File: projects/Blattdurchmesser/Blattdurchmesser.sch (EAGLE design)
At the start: 14 parts, among them K1 TX2_RELAY", U1 ARDUINOR3-DIMENSION

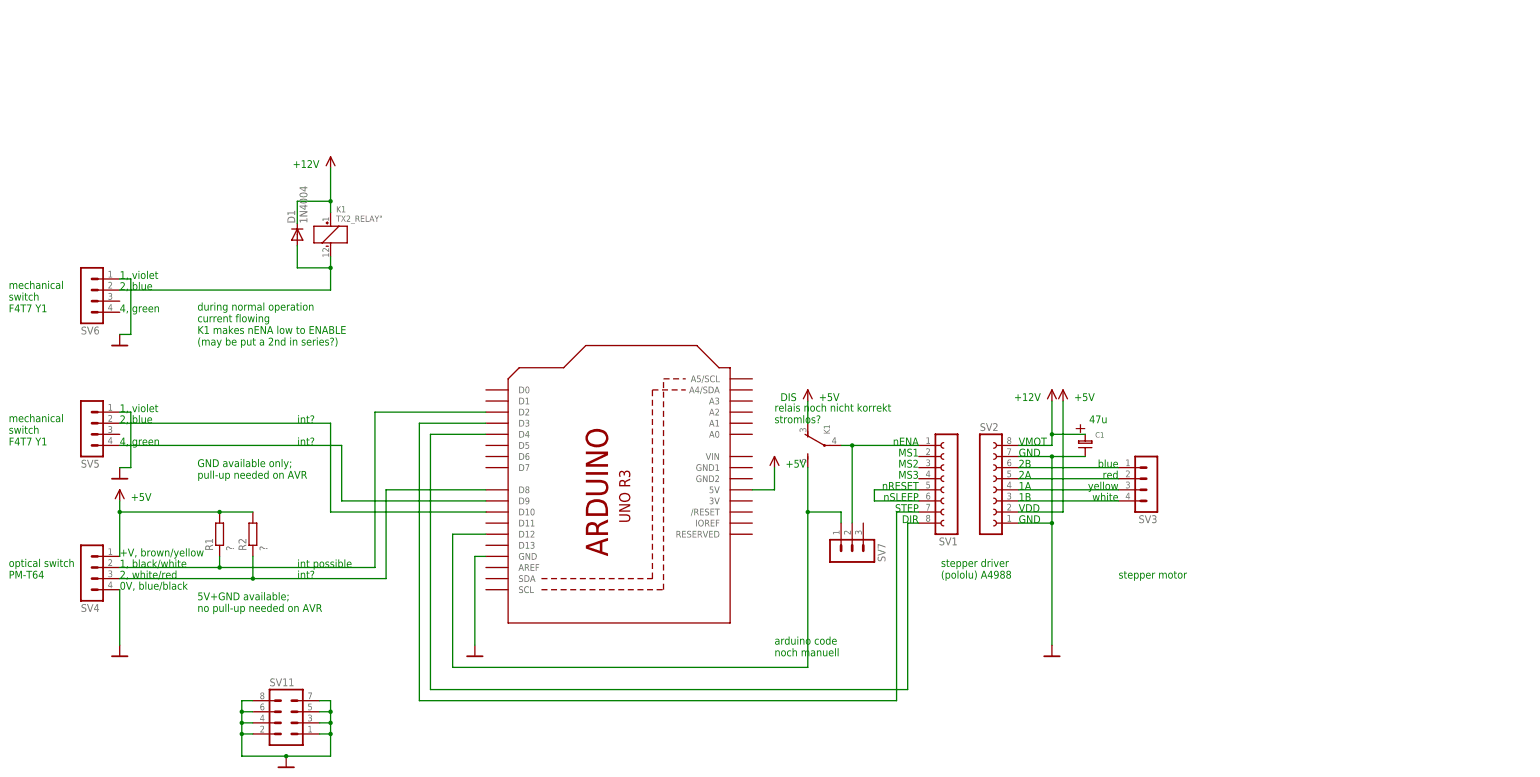
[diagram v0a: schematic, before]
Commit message: improvement; * replace arduino part/footprint by one that does                not have milling slots              * avoid using a relais as it has disadvantages
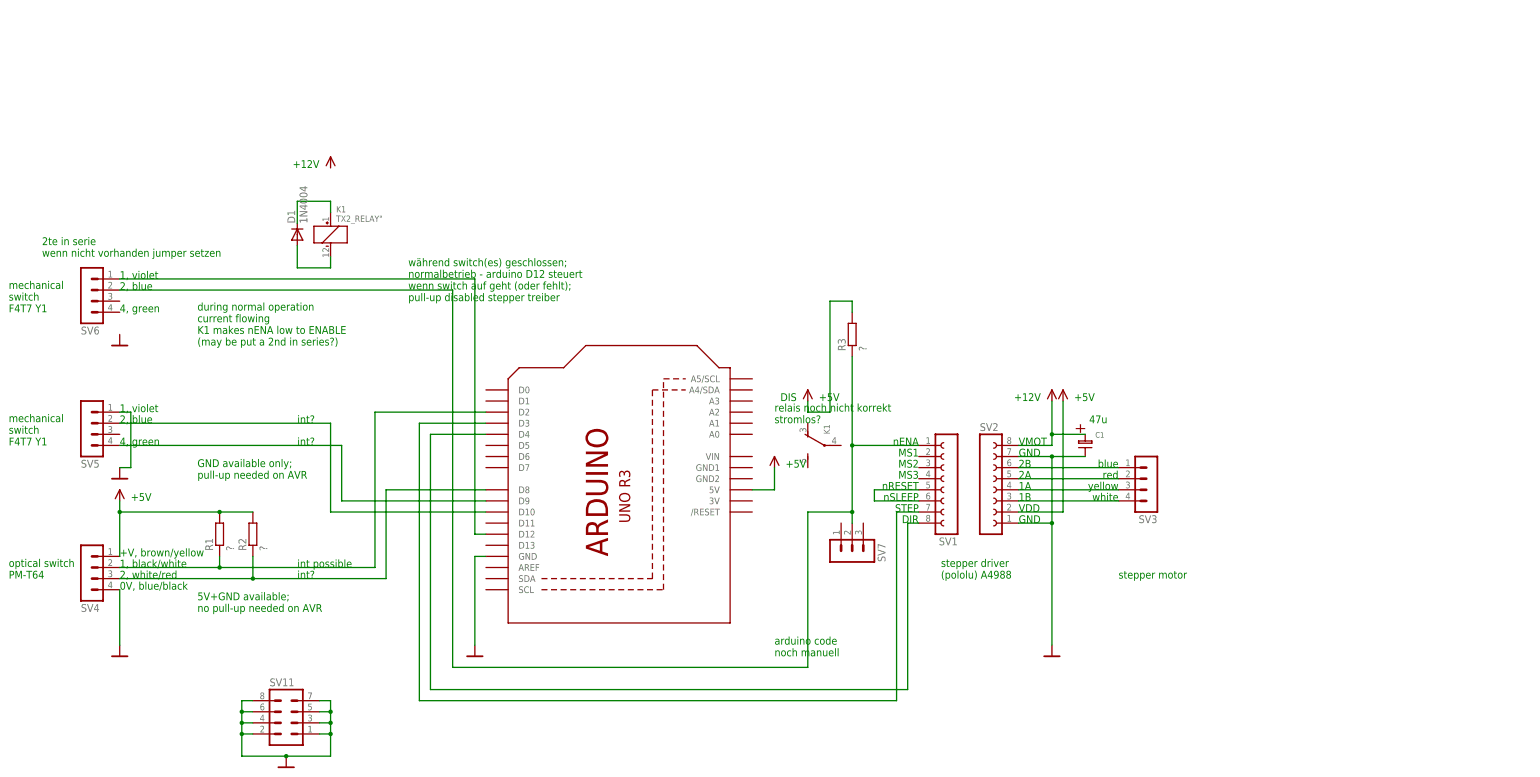
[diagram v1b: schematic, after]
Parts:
- removed U1: ARDUINOR3-DIMENSION, adafruit:ARDUINOR3-DIMENSION
- added Q1: ARDUINOR3-NOIOREF-NOTEXT, adafruit:ARDUINOR3-NOIOREF-NOTEXT
- added R3: ?, rcl:R-EU_0207/10
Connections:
- removed net N$10: K1TX2_SWITCH.P, SV1.1, SV7.2
- new net N$16: D1.C, K1TX2_COIL.+
- new net N$8: D1.A, K1TX2_COIL.-
- net +12V: no longer D1.C, K1TX2_COIL.+
- net +5V: now also Q1.5V, R3.2; no longer K1TX2_SWITCH.O, U1.5V
- net GND: now also Q1.GND; no longer SV6.1, U1.GND
- net N$1: now also Q1.D4; no longer U1.D4
- net N$11: now also Q1.D12, SV6.1; no longer D1.A, K1TX2_COIL.-, SV6.2
- net N$12: now also Q1.D10; no longer U1.D10
- net N$13: now also Q1.D9; no longer U1.D9
- net N$14: now also R3.1, SV1.1, SV6.2, SV7.2; no longer K1TX2_SWITCH.S, SV7.1, U1.D12
- net N$15: now also Q1.D2; no longer U1.D2
- net N$2: now also Q1.D3; no longer U1.D3
- net N$9: now also Q1.D8; no longer U1.D8
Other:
- note added: "2te in serie wenn nicht vorhanden jumper setzen"
- note added: "während switch(es) geschlossen; normalbetrieb - arduino D12 steuert wenn switch auf geht (oder fehlt); pull-up disabled stepper treiber"
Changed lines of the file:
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@@
 </classes>
 <parts>
-<part name="U1" library="adafruit" deviceset="ARDUINOR3" device="-DIMENSION"/>
 <part name="K1" library="relay" deviceset="TX2_RELAY" device="&quot;"/>
 <part name="SV1" library="con-lsta" deviceset="FE08-1" device=""/>
@@
 <part name="D1" library="diode" deviceset="1N4004" device=""/>
 <part name="SV7" library="con-lstb" deviceset="MA03-1" device=""/>
+<part name="R3" library="rcl" deviceset="R-EU_" device="0207/10" value="?"/>
+<part name="Q1" library="adafruit" deviceset="ARDUINOR3-NOIOREF" device="-NOTEXT"/>
 </parts>
 <sheets>
@@
 <text x="119.38" y="50.8" size="1.778" layer="91">relais noch nicht korrekt
 stromlos?</text>
+<text x="35.56" y="78.74" size="1.778" layer="91">während switch(es) geschlossen;
+normalbetrieb - arduino D12 steuert
+wenn switch auf geht (oder fehlt);
+pull-up disabled stepper treiber</text>
+<text x="-48.26" y="88.9" size="1.778" layer="91">2te in serie
+wenn nicht vorhanden jumper setzen</text>
 </plain>
 <instances>
-<instance part="U1" gate="G$1" x="83.82" y="38.1" rot="R90"/>
 <instance part="K1" gate="TX2_COIL" x="17.78" y="93.98"/>
 <instance part="K1" gate="TX2_SWITCH" x="132.08" y="45.72" rot="R90"/>
@@
 <instance part="D1" gate="1" x="10.16" y="93.98" rot="R90"/>
 <instance part="SV7" gate="G$1" x="137.16" y="20.32" rot="MR90"/>
+<instance part="R3" gate="G$1" x="137.16" y="71.12" rot="R90"/>
+<instance part="Q1" gate="G$1" x="83.82" y="38.1" rot="R90"/>
 </instances>
 <busses>
@@
 <pinref part="U$3" gate="1" pin="GND"/>
 <wire x1="50.8" y1="0" x2="50.8" y2="20.32" width="0.1524" layer="91"/>
-<pinref part="U1" gate="G$1" pin="GND"/>
 <wire x1="50.8" y1="20.32" x2="53.34" y2="20.32" width="0.1524" layer="91"/>
+<pinref part="Q1" gate="G$1" pin="GND"/>
 </segment>
 <segment>
@@
 <junction x="7.62" y="-25.4"/>
 </segment>
-<segment>
-<pinref part="SV6" gate="1" pin="1"/>
-<wire x1="-30.48" y1="83.82" x2="-27.94" y2="83.82" width="0.1524" layer="91"/>
-<wire x1="-27.94" y1="83.82" x2="-27.94" y2="71.12" width="0.1524" layer="91"/>
-<pinref part="U$12" gate="1" pin="GND"/>
-<wire x1="-27.94" y1="71.12" x2="-30.48" y2="71.12" width="0.1524" layer="91"/>
-</segment>
 </net>
 <net name="+5V" class="0">
@@
 </segment>
 <segment>
-<pinref part="U1" gate="G$1" pin="5V"/>
 <pinref part="U$7" gate="1" pin="+5V"/>
-<wire x1="114.3" y1="35.56" x2="119.38" y2="35.56" width="0.1524" layer="91"/>
 <wire x1="119.38" y1="35.56" x2="119.38" y2="40.64" width="0.1524" layer="91"/>
+<pinref part="Q1" gate="G$1" pin="5V"/>
+<wire x1="119.38" y1="35.56" x2="114.3" y2="35.56" width="0.1524" layer="91"/>
 </segment>
 <segment>
@@
 <segment>
 <pinref part="U$8" gate="1" pin="+5V"/>
-<pinref part="K1" gate="TX2_SWITCH" pin="O"/>
-<wire x1="127" y1="55.88" x2="127" y2="50.8" width="0.1524" layer="91"/>
+<wire x1="127" y1="55.88" x2="127" y2="53.34" width="0.1524" layer="91"/>
+<wire x1="127" y1="53.34" x2="132.08" y2="53.34" width="0.1524" layer="91"/>
+<wire x1="132.08" y1="53.34" x2="132.08" y2="78.74" width="0.1524" layer="91"/>
+<pinref part="R3" gate="G$1" pin="2"/>
+<wire x1="132.08" y1="78.74" x2="137.16" y2="78.74" width="0.1524" layer="91"/>
+<wire x1="137.16" y1="78.74" x2="137.16" y2="76.2" width="0.1524" layer="91"/>
 </segment>
 </net>
@@
 <junction x="182.88" y="48.26"/>
 </segment>
-<segment>
-<pinref part="K1" gate="TX2_COIL" pin="+"/>
-<pinref part="U$13" gate="1" pin="+12V"/>
-<wire x1="17.78" y1="99.06" x2="17.78" y2="101.6" width="0.1524" layer="91"/>
-<pinref part="D1" gate="1" pin="C"/>
-<wire x1="17.78" y1="101.6" x2="17.78" y2="109.22" width="0.1524" layer="91"/>
-<wire x1="10.16" y1="96.52" x2="10.16" y2="101.6" width="0.1524" layer="91"/>
-<wire x1="10.16" y1="101.6" x2="17.78" y2="101.6" width="0.1524" layer="91"/>
-<junction x="17.78" y="101.6"/>
-</segment>
 </net>
 <net name="N$3" class="0">
@@
 <wire x1="149.86" y1="-10.16" x2="40.64" y2="-10.16" width="0.1524" layer="91"/>
 <wire x1="40.64" y1="-10.16" x2="40.64" y2="48.26" width="0.1524" layer="91"/>
-<pinref part="U1" gate="G$1" pin="D4"/>
 <wire x1="40.64" y1="48.26" x2="53.34" y2="48.26" width="0.1524" layer="91"/>
+<pinref part="Q1" gate="G$1" pin="D4"/>
 </segment>
 </net>
@@
 <wire x1="147.32" y1="-12.7" x2="38.1" y2="-12.7" width="0.1524" layer="91"/>
 <wire x1="38.1" y1="-12.7" x2="38.1" y2="50.8" width="0.1524" layer="91"/>
-<pinref part="U1" gate="G$1" pin="D3"/>
+<pinref part="Q1" gate="G$1" pin="D3"/>
 <wire x1="38.1" y1="50.8" x2="53.34" y2="50.8" width="0.1524" layer="91"/>
 </segment>
@@
 <wire x1="0" y1="15.24" x2="30.48" y2="15.24" width="0.1524" layer="91"/>
 <wire x1="30.48" y1="15.24" x2="30.48" y2="35.56" width="0.1524" layer="91"/>
-<pinref part="U1" gate="G$1" pin="D8"/>
 <wire x1="30.48" y1="35.56" x2="53.34" y2="35.56" width="0.1524" layer="91"/>
+<pinref part="Q1" gate="G$1" pin="D8"/>
 </segment>
 </net>
@@
 <wire x1="-30.48" y1="50.8" x2="17.78" y2="50.8" width="0.1524" layer="91"/>
 <wire x1="17.78" y1="50.8" x2="17.78" y2="30.48" width="0.1524" layer="91"/>
-<pinref part="U1" gate="G$1" pin="D10"/>
+<pinref part="Q1" gate="G$1" pin="D10"/>
 <wire x1="17.78" y1="30.48" x2="53.34" y2="30.48" width="0.1524" layer="91"/>
 </segment>
@@
 <pinref part="SV5" gate="1" pin="4"/>
 <wire x1="-30.48" y1="45.72" x2="20.32" y2="45.72" width="0.1524" layer="91"/>
-<pinref part="U1" gate="G$1" pin="D9"/>
-<wire x1="53.34" y1="33.02" x2="20.32" y2="33.02" width="0.1524" layer="91"/>
 <wire x1="20.32" y1="33.02" x2="20.32" y2="45.72" width="0.1524" layer="91"/>
-</segment>
-</net>
-<net name="N$11" class="0">
-<segment>
-<pinref part="SV6" gate="1" pin="2"/>
-<wire x1="-30.48" y1="81.28" x2="17.78" y2="81.28" width="0.1524" layer="91"/>
-<pinref part="K1" gate="TX2_COIL" pin="-"/>
-<wire x1="17.78" y1="81.28" x2="17.78" y2="86.36" width="0.1524" layer="91"/>
-<pinref part="D1" gate="1" pin="A"/>
-<wire x1="17.78" y1="86.36" x2="17.78" y2="88.9" width="0.1524" layer="91"/>
-<wire x1="10.16" y1="91.44" x2="10.16" y2="86.36" width="0.1524" layer="91"/>
-<wire x1="10.16" y1="86.36" x2="17.78" y2="86.36" width="0.1524" layer="91"/>
-<junction x="17.78" y="86.36"/>
+<pinref part="Q1" gate="G$1" pin="D9"/>
+<wire x1="20.32" y1="33.02" x2="53.34" y2="33.02" width="0.1524" layer="91"/>
 </segment>
 </net>
 <net name="N$14" class="0">
 <segment>
-<wire x1="127" y1="40.64" x2="127" y2="30.48" width="0.1524" layer="91"/>
 <wire x1="127" y1="30.48" x2="127" y2="-5.08" width="0.1524" layer="91"/>
 <wire x1="127" y1="-5.08" x2="45.72" y2="-5.08" width="0.1524" layer="91"/>
-<wire x1="45.72" y1="-5.08" x2="45.72" y2="25.4" width="0.1524" layer="91"/>
-<pinref part="U1" gate="G$1" pin="D12"/>
-<wire x1="45.72" y1="25.4" x2="53.34" y2="25.4" width="0.1524" layer="91"/>
-<pinref part="K1" gate="TX2_SWITCH" pin="S"/>
-<pinref part="SV7" gate="G$1" pin="1"/>
-<wire x1="134.62" y1="27.94" x2="134.62" y2="30.48" width="0.1524" layer="91"/>
-<wire x1="134.62" y1="30.48" x2="127" y2="30.48" width="0.1524" layer="91"/>
-<junction x="127" y="30.48"/>
-</segment>
-</net>
-<net name="N$10" class="0">
-<segment>
+<wire x1="137.16" y1="30.48" x2="127" y2="30.48" width="0.1524" layer="91"/>
+<pinref part="SV6" gate="1" pin="2"/>
+<wire x1="-30.48" y1="81.28" x2="45.72" y2="81.28" width="0.1524" layer="91"/>
+<wire x1="45.72" y1="81.28" x2="45.72" y2="-5.08" width="0.1524" layer="91"/>
 <pinref part="SV1" gate="G$1" pin="1"/>
 <wire x1="152.4" y1="45.72" x2="137.16" y2="45.72" width="0.1524" layer="91"/>
-<pinref part="K1" gate="TX2_SWITCH" pin="P"/>
 <pinref part="SV7" gate="G$1" pin="2"/>
-<wire x1="137.16" y1="45.72" x2="134.62" y2="45.72" width="0.1524" layer="91"/>
-<wire x1="137.16" y1="27.94" x2="137.16" y2="45.72" width="0.1524" layer="91"/>
+<wire x1="137.16" y1="27.94" x2="137.16" y2="30.48" width="0.1524" layer="91"/>
+<pinref part="R3" gate="G$1" pin="1"/>
+<wire x1="137.16" y1="30.48" x2="137.16" y2="45.72" width="0.1524" layer="91"/>
+<wire x1="137.16" y1="66.04" x2="137.16" y2="45.72" width="0.1524" layer="91"/>
 <junction x="137.16" y="45.72"/>
+<junction x="137.16" y="30.48"/>
 </segment>
 </net>
@@
 <wire x1="-7.62" y1="17.78" x2="-7.62" y2="20.32" width="0.1524" layer="91"/>
 <wire x1="27.94" y1="17.78" x2="27.94" y2="53.34" width="0.1524" layer="91"/>
-<pinref part="U1" gate="G$1" pin="D2"/>
 <wire x1="27.94" y1="53.34" x2="53.34" y2="53.34" width="0.1524" layer="91"/>
 <wire x1="-7.62" y1="17.78" x2="27.94" y2="17.78" width="0.1524" layer="91"/>
 <junction x="-7.62" y="17.78"/>
-</segment>
-</net>
+<pinref part="Q1" gate="G$1" pin="D2"/>
+</segment>
+</net>
+<net name="N$8" class="0">
+<segment>
+<pinref part="K1" gate="TX2_COIL" pin="-"/>
+<wire x1="17.78" y1="86.36" x2="17.78" y2="88.9" width="0.1524" layer="91"/>
+<pinref part="D1" gate="1" pin="A"/>
+<wire x1="10.16" y1="91.44" x2="10.16" y2="86.36" width="0.1524" layer="91"/>
+<wire x1="10.16" y1="86.36" x2="17.78" y2="86.36" width="0.1524" layer="91"/>
+</segment>
+</net>
+<net name="N$16" class="0">
+<segment>
+<pinref part="K1" gate="TX2_COIL" pin="+"/>
+<wire x1="17.78" y1="99.06" x2="17.78" y2="101.6" width="0.1524" layer="91"/>
+<pinref part="D1" gate="1" pin="C"/>
+<wire x1="10.16" y1="96.52" x2="10.16" y2="101.6" width="0.1524" layer="91"/>
+<wire x1="10.16" y1="101.6" x2="17.78" y2="101.6" width="0.1524" layer="91"/>
+</segment>
+</net>
+<net name="N$11" class="0">
+<segment>
+<wire x1="50.8" y1="25.4" x2="50.8" y2="83.82" width="0.1524" layer="91"/>
+<pinref part="SV6" gate="1" pin="1"/>
+<wire x1="50.8" y1="83.82" x2="-30.48" y2="83.82" width="0.1524" layer="91"/>
+<pinref part="Q1" gate="G$1" pin="D12"/>
+<wire x1="50.8" y1="25.4" x2="53.34" y2="25.4" width="0.1524" layer="91"/>
+</segment>
+</net>

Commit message: improvement; * pcb routed for 1st time
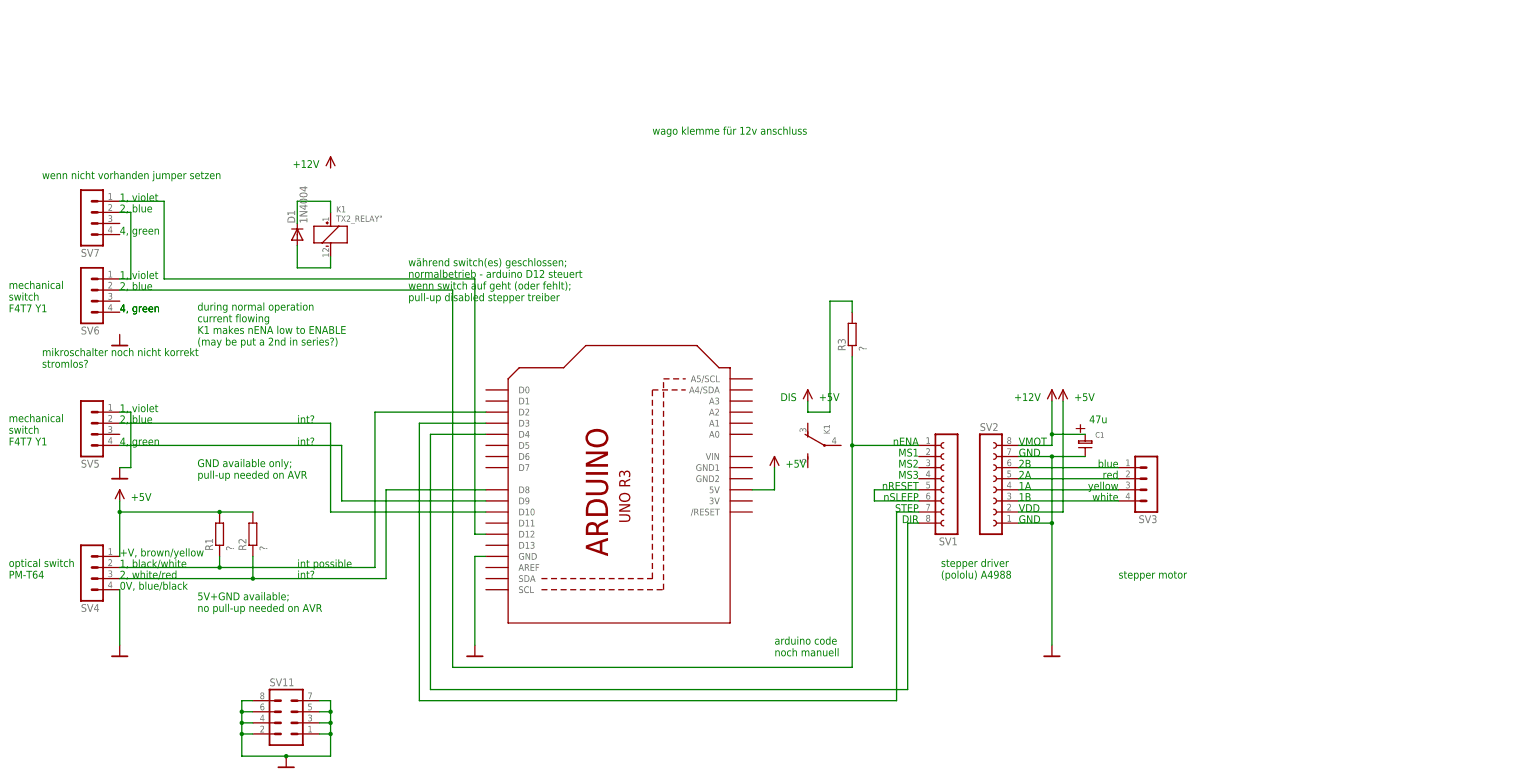
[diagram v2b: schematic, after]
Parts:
- SV7: device con-lstb:MA03-1 -> con-lstb:MA04-1
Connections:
- new net N$10: SV6.1, SV7.2
- net N$11: now also SV7.1; no longer SV6.1
- net N$14: no longer SV7.2
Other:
- note added: "mikroschalter noch nicht korrekt stromlos?"
- note added: "wago klemme für 12v anschluss"
- note added: "wenn nicht vorhanden jumper setzen"
- note removed: "2te in serie wenn nicht vorhanden jumper setzen"
- note removed: "relais noch nicht korrekt stromlos?"
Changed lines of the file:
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@@
 <part name="U$13" library="Netze" deviceset="+12V" device=""/>
 <part name="D1" library="diode" deviceset="1N4004" device=""/>
-<part name="SV7" library="con-lstb" deviceset="MA03-1" device=""/>
 <part name="R3" library="rcl" deviceset="R-EU_" device="0207/10" value="?"/>
 <part name="Q1" library="adafruit" deviceset="ARDUINOR3-NOIOREF" device="-NOTEXT"/>
+<part name="SV7" library="con-lstb" deviceset="MA04-1" device=""/>
 </parts>
 <sheets>
@@
 <text x="119.38" y="-2.54" size="1.778" layer="91">arduino code
 noch manuell</text>
-<text x="119.38" y="50.8" size="1.778" layer="91">relais noch nicht korrekt
+<text x="-48.26" y="63.5" size="1.778" layer="91">mikroschalter noch nicht korrekt
 stromlos?</text>
 <text x="35.56" y="78.74" size="1.778" layer="91">während switch(es) geschlossen;
@@
 wenn switch auf geht (oder fehlt);
 pull-up disabled stepper treiber</text>
-<text x="-48.26" y="88.9" size="1.778" layer="91">2te in serie
-wenn nicht vorhanden jumper setzen</text>
+<text x="-48.26" y="106.68" size="1.778" layer="91">wenn nicht vorhanden jumper setzen</text>
+<text x="-30.48" y="101.6" size="1.778" layer="91">1, violet</text>
+<text x="-30.48" y="99.06" size="1.778" layer="91">2, blue</text>
+<text x="-30.48" y="76.2" size="1.778" layer="91">4, green</text>
+<text x="-30.48" y="93.98" size="1.778" layer="91">4, green</text>
+<text x="91.44" y="116.84" size="1.778" layer="91">wago klemme für 12v anschluss</text>
 </plain>
 <instances>
@@
 <instance part="U$13" gate="1" x="17.78" y="104.14"/>
 <instance part="D1" gate="1" x="10.16" y="93.98" rot="R90"/>
-<instance part="SV7" gate="G$1" x="137.16" y="20.32" rot="MR90"/>
 <instance part="R3" gate="G$1" x="137.16" y="71.12" rot="R90"/>
 <instance part="Q1" gate="G$1" x="83.82" y="38.1" rot="R90"/>
+<instance part="SV7" gate="1" x="-38.1" y="96.52" rot="MR180"/>
 </instances>
 <busses>
@@
 <net name="N$14" class="0">
 <segment>
-<wire x1="127" y1="30.48" x2="127" y2="-5.08" width="0.1524" layer="91"/>
-<wire x1="127" y1="-5.08" x2="45.72" y2="-5.08" width="0.1524" layer="91"/>
-<wire x1="137.16" y1="30.48" x2="127" y2="30.48" width="0.1524" layer="91"/>
+<wire x1="137.16" y1="45.72" x2="137.16" y2="-5.08" width="0.1524" layer="91"/>
+<wire x1="137.16" y1="-5.08" x2="45.72" y2="-5.08" width="0.1524" layer="91"/>
 <pinref part="SV6" gate="1" pin="2"/>
 <wire x1="-30.48" y1="81.28" x2="45.72" y2="81.28" width="0.1524" layer="91"/>
@@
 <pinref part="SV1" gate="G$1" pin="1"/>
 <wire x1="152.4" y1="45.72" x2="137.16" y2="45.72" width="0.1524" layer="91"/>
-<pinref part="SV7" gate="G$1" pin="2"/>
-<wire x1="137.16" y1="27.94" x2="137.16" y2="30.48" width="0.1524" layer="91"/>
 <pinref part="R3" gate="G$1" pin="1"/>
-<wire x1="137.16" y1="30.48" x2="137.16" y2="45.72" width="0.1524" layer="91"/>
 <wire x1="137.16" y1="66.04" x2="137.16" y2="45.72" width="0.1524" layer="91"/>
 <junction x="137.16" y="45.72"/>
-<junction x="137.16" y="30.48"/>
 </segment>
 </net>
@@
 <segment>
 <wire x1="50.8" y1="25.4" x2="50.8" y2="83.82" width="0.1524" layer="91"/>
-<pinref part="SV6" gate="1" pin="1"/>
-<wire x1="50.8" y1="83.82" x2="-30.48" y2="83.82" width="0.1524" layer="91"/>
+<wire x1="50.8" y1="83.82" x2="-20.32" y2="83.82" width="0.1524" layer="91"/>
 <pinref part="Q1" gate="G$1" pin="D12"/>
 <wire x1="50.8" y1="25.4" x2="53.34" y2="25.4" width="0.1524" layer="91"/>
-</segment>
-</net>
+<wire x1="-20.32" y1="83.82" x2="-20.32" y2="101.6" width="0.1524" layer="91"/>
+<pinref part="SV7" gate="1" pin="1"/>
+<wire x1="-20.32" y1="101.6" x2="-30.48" y2="101.6" width="0.1524" layer="91"/>
+</segment>
+</net>
+<net name="N$10" class="0">
+<segment>
+<pinref part="SV7" gate="1" pin="2"/>
+<wire x1="-30.48" y1="99.06" x2="-27.94" y2="99.06" width="0.1524" layer="91"/>
+<wire x1="-27.94" y1="99.06" x2="-27.94" y2="83.82" width="0.1524" layer="91"/>
+<pinref part="SV6" gate="1" pin="1"/>
+<wire x1="-27.94" y1="83.82" x2="-30.48" y2="83.82" width="0.1524" layer="91"/>
+</segment>
+</net>
